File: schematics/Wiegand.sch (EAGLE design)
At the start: 66 parts, among them IC1 MC33269ST-3.3T3, J1 AVR_SPI_PRG_6NS, Q1 NTR1P02T1G, Q2 NTR1P02T1G, U1 ATMEGA168, U2 RS485_SP491, U4 MOC3063, U5 MOC3063, U6 MOC3063, U7 MOC3063, U8 MOC3063, U9 MOC3063, Y1 16Mhz

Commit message: minor changes to board, adding firmware and eagleup render
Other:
- note added: "- 100ohm resistor on head: B---A - 100ohm resistor on slave: Y---Z, B---A CONNECTIONS: - Head-Z --- Slave-B - Head-Y --- Slave-A - Head-A --- Slave-Y - Head-B --- Slave-Z"
- note added: "- add pullup resistors to D0 and D1 (use internal?) - add 0.1uf decoup ceramic near 5v headers - fix and annotate terminal node jumpers and resistors"
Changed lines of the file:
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@@
 <setting verticaltext="up"/>
 </settings>
-<grid distance="0.1" unitdist="inch" unit="inch" style="lines" multiple="1" display="no" altdistance="0.01" altunitdist="inch" altunit="inch"/>
+<grid distance="100" unitdist="mil" unit="mil" style="lines" multiple="1" display="no" altdistance="50" altunitdist="mil" altunit="mil"/>
 <layers>
 <layer number="1" name="Top" color="4" fill="1" visible="no" active="no"/>
@@
 <layer number="108" name="tplace-old" color="10" fill="1" visible="yes" active="yes"/>
 <layer number="109" name="ref-old" color="11" fill="1" visible="yes" active="yes"/>
-<layer number="110" name="fp0" color="7" fill="1" visible="no" active="yes"/>
+<layer number="110" name="fp0" color="7" fill="1" visible="yes" active="yes"/>
 <layer number="116" name="Patch_BOT" color="9" fill="4" visible="yes" active="yes"/>
 <layer number="121" name="_tsilk" color="7" fill="1" visible="yes" active="yes"/>
 <layer number="122" name="_bsilk" color="7" fill="1" visible="yes" active="yes"/>
-<layer number="123" name="tTestmark" color="7" fill="1" visible="no" active="yes"/>
-<layer number="124" name="bTestmark" color="7" fill="1" visible="no" active="yes"/>
-<layer number="125" name="_tNames" color="7" fill="1" visible="no" active="yes"/>
+<layer number="123" name="tTestmark" color="7" fill="1" visible="yes" active="yes"/>
+<layer number="124" name="bTestmark" color="7" fill="1" visible="yes" active="yes"/>
+<layer number="125" name="_tNames" color="7" fill="1" visible="yes" active="yes"/>
 <layer number="131" name="prix" color="7" fill="1" visible="yes" active="yes"/>
 <layer number="132" name="test" color="7" fill="1" visible="yes" active="yes"/>
-<layer number="144" name="Drill_legend" color="7" fill="1" visible="no" active="yes"/>
+<layer number="144" name="Drill_legend" color="7" fill="1" visible="yes" active="yes"/>
 <layer number="151" name="HeatSink" color="7" fill="1" visible="yes" active="yes"/>
-<layer number="199" name="Contour" color="7" fill="1" visible="no" active="yes"/>
+<layer number="199" name="Contour" color="7" fill="1" visible="yes" active="yes"/>
 <layer number="200" name="200bmp" color="1" fill="10" visible="no" active="no"/>
 <layer number="201" name="201bmp" color="2" fill="1" visible="no" active="no"/>
@@
 <layer number="207" name="207bmp" color="8" fill="10" visible="yes" active="yes"/>
 <layer number="208" name="208bmp" color="9" fill="10" visible="yes" active="yes"/>
-<layer number="209" name="209bmp" color="7" fill="1" visible="no" active="yes"/>
-<layer number="210" name="210bmp" color="7" fill="1" visible="no" active="yes"/>
-<layer number="211" name="211bmp" color="7" fill="1" visible="no" active="yes"/>
-<layer number="212" name="212bmp" color="7" fill="1" visible="no" active="yes"/>
-<layer number="213" name="213bmp" color="7" fill="1" visible="no" active="yes"/>
-<layer number="214" name="214bmp" color="7" fill="1" visible="no" active="yes"/>
-<layer number="215" name="215bmp" color="7" fill="1" visible="no" active="yes"/>
-<layer number="216" name="216bmp" color="7" fill="1" visible="no" active="yes"/>
+<layer number="209" name="209bmp" color="7" fill="1" visible="yes" active="yes"/>
+<layer number="210" name="210bmp" color="7" fill="1" visible="yes" active="yes"/>
+<layer number="211" name="211bmp" color="7" fill="1" visible="yes" active="yes"/>
+<layer number="212" name="212bmp" color="7" fill="1" visible="yes" active="yes"/>
+<layer number="213" name="213bmp" color="7" fill="1" visible="yes" active="yes"/>
+<layer number="214" name="214bmp" color="7" fill="1" visible="yes" active="yes"/>
+<layer number="215" name="215bmp" color="7" fill="1" visible="yes" active="yes"/>
+<layer number="216" name="216bmp" color="7" fill="1" visible="yes" active="yes"/>
 <layer number="217" name="217bmp" color="18" fill="1" visible="no" active="no"/>
 <layer number="218" name="218bmp" color="19" fill="1" visible="no" active="no"/>
@@
 <text x="139.7" y="162.56" size="1.778" layer="91" rot="R270">FIRST NODE</text>
 <text x="203.2" y="157.48" size="1.778" layer="91" rot="R270">LAST NODE</text>
+<text x="287.02" y="261.62" size="5.08" layer="91" align="bottom-right">- add pullup resistors to D0 and D1 (use internal?)
+- add 0.1uf decoup ceramic near 5v headers
+- fix and annotate terminal node jumpers and resistors</text>
+<text x="307.34" y="17.78" size="5.08" layer="91">- 100ohm resistor on head: B---A
+- 100ohm resistor on slave: Y---Z, B---A
+CONNECTIONS:
+- Head-Z --- Slave-B
+- Head-Y --- Slave-A
+- Head-A --- Slave-Y
+- Head-B --- Slave-Z</text>
 </plain>
 <instances>

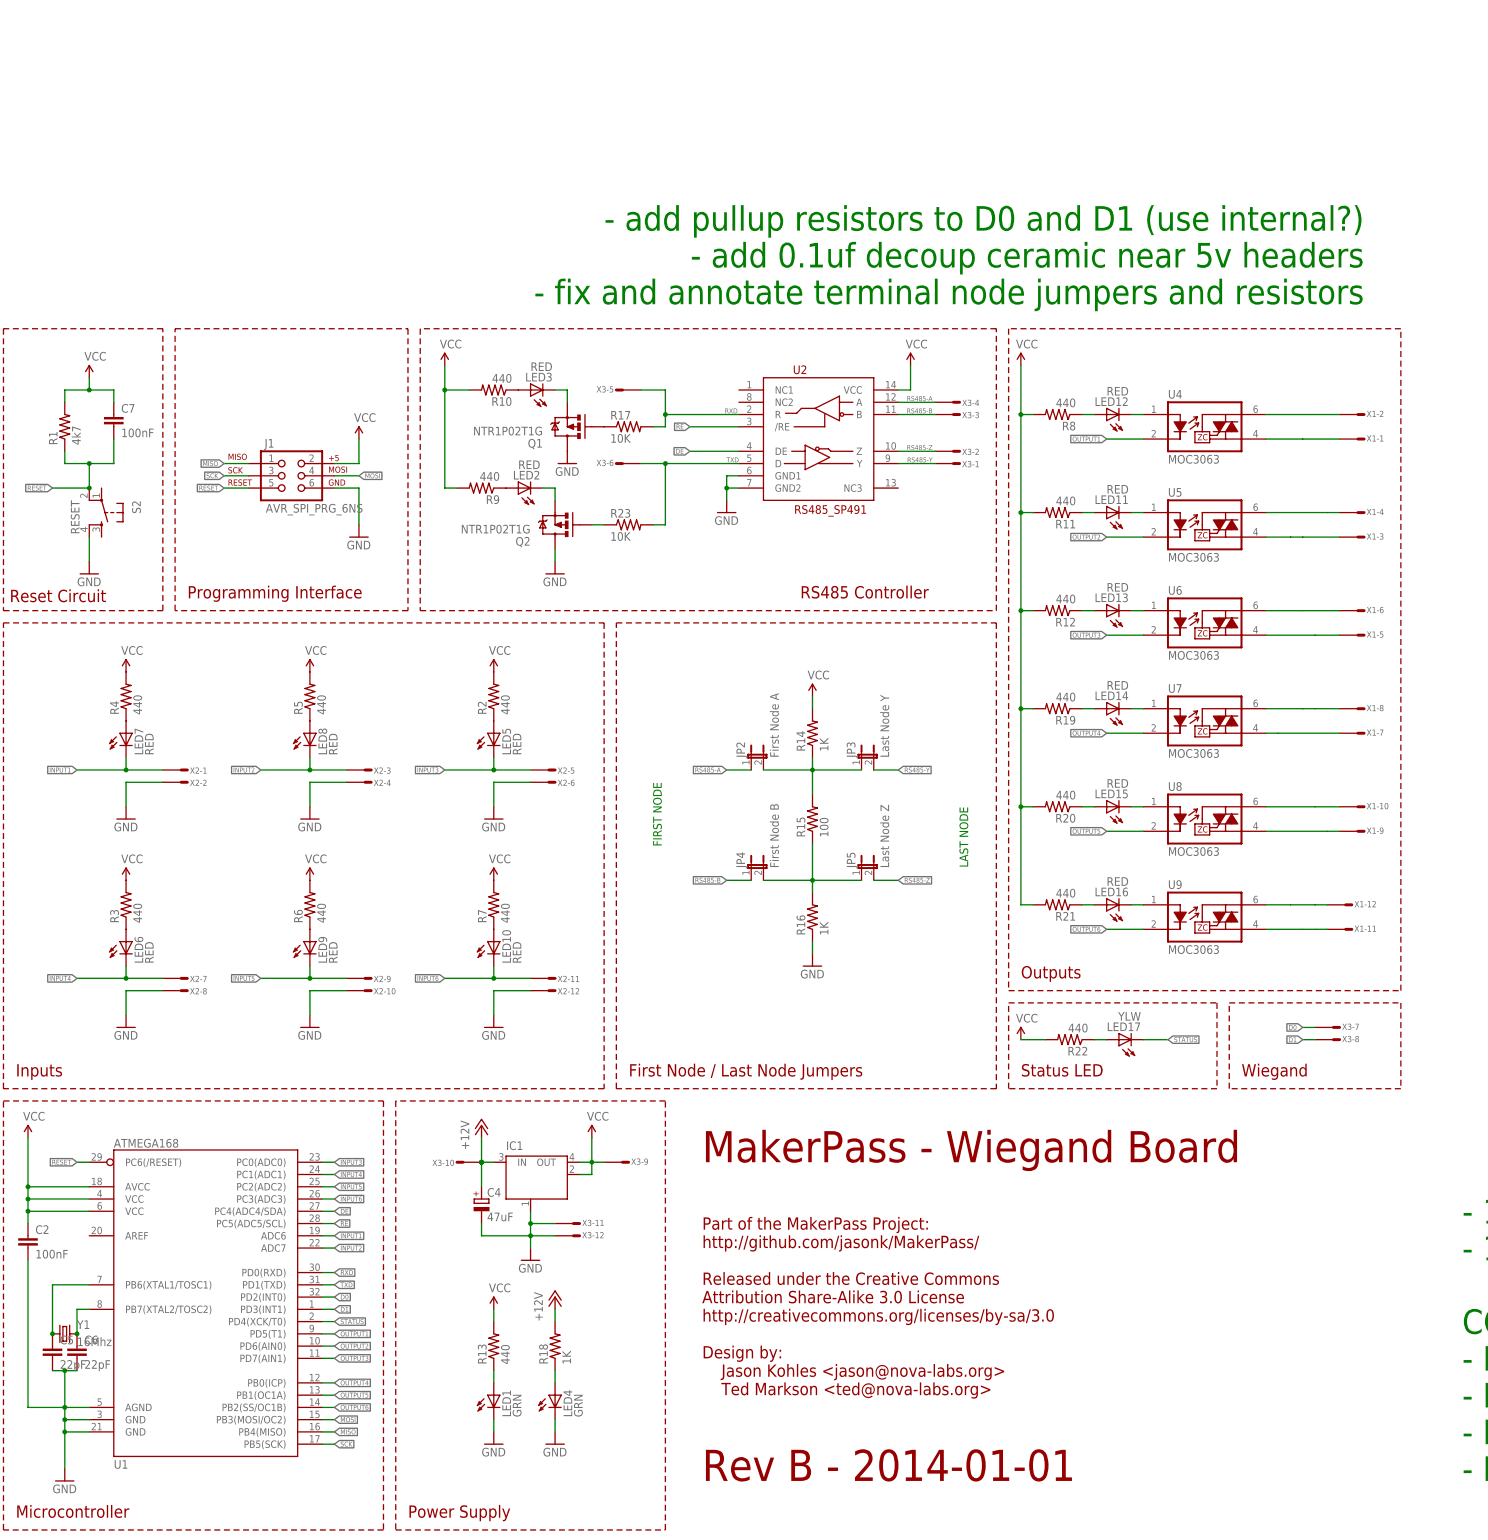
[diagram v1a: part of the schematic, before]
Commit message: minor edits to brd, rerendered eagleup model
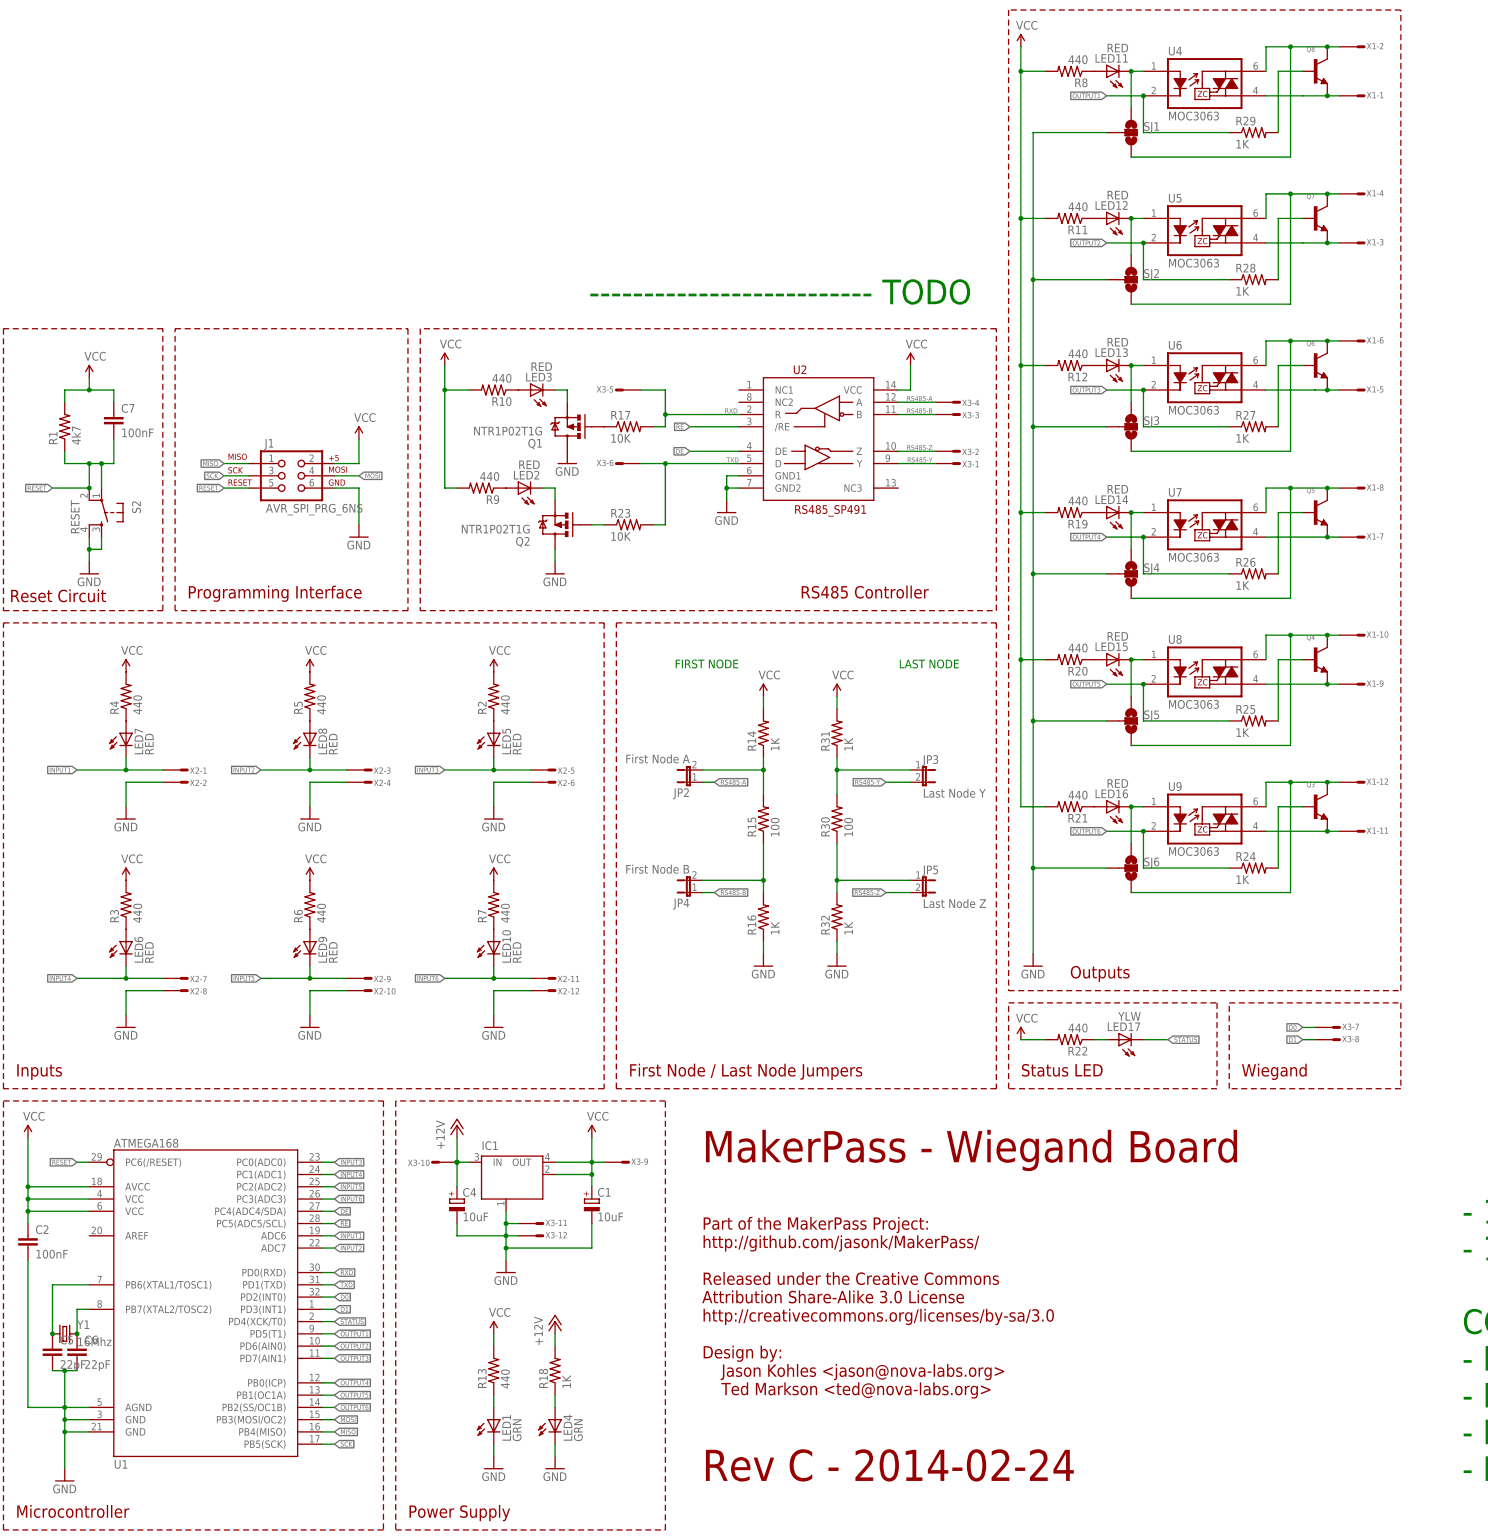
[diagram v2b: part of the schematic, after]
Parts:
- added C1: 10uF, rcl:CPOL-EUD
- added Q3, Q4, Q5, Q6, Q7, Q8: (no value), LumisenseV6:NPN-BEC-SOT23-3
- added R24, R25, R26, R27, R28, R29, R31, R32: 1K, SparkFun:RESISTOR0603-RES
- added R30: 100, SparkFun:RESISTOR0603-RES
- added SJ1, SJ2, SJ3, SJ4, SJ5, SJ6: (no value), SparkFun-Passives:SOLDERJUMPER_2WAYS
- C4: value 47uF -> 10uF; MFG_PN EMVA250ADA470MF55G -> EMVA250ADA100MD55G
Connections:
- removed net N$17: U4.T2, X1-1.S
- new net N$43: Q4.B, R25.2
- new net N$435: Q3.B, R24.2
- new net N$44: Q5.B, R26.2
- new net N$48: Q6.B, R27.2
- new net N$49: Q7.B, R28.2
- new net N$50: Q8.B, R29.2
- new net N$51: JP2.2, R14.1, R15.2
- new net N$52: JP4.2, R15.1, R16.2
- new net N$53: Q8.E, U4.T2, X1-1.S
- net GND: now also C1.-, R32.1, S2.3, SJ1.2, SJ2.2, SJ3.2, SJ4.2, SJ5.2, SJ6.2
- net N$15: now also LED11.C, SJ1.1; no longer LED12.C
- net N$16: now also LED11.A; no longer LED12.A
- net N$18: now also Q8.C, SJ1.3
- net N$19: now also Q7.E
- net N$20: now also Q7.C, SJ2.3
- net N$21: now also LED12.A; no longer LED11.A
- net N$22: now also LED12.C, SJ2.1; no longer LED11.C
- net N$23: now also Q6.E
- net N$24: now also Q6.C, SJ3.3
- net N$28: now also SJ3.1
- net N$29: now also Q5.E
- net N$3: now also Q4.E
- net N$30: now also Q5.C, SJ4.3
- net N$32: now also SJ4.1
- net N$36: now also SJ5.1
- net N$37: now also Q3.C, SJ6.3, U9.T1, X1-12.S; no longer U9.T2, X1-11.S
- net N$38: now also Q3.E, U9.T2, X1-11.S; no longer U9.T1, X1-12.S
- net N$4: now also Q4.C, SJ5.3
- net N$40: now also SJ6.1
- net N$6: now also R30.1, R32.2; no longer JP4.2, R15.1, R16.2
- net N$7: now also R30.2, R31.1; no longer JP2.2, R14.1, R15.2
- net OUTPUT1: now also R29.1
- net OUTPUT2: now also R28.1
- net OUTPUT3: now also R27.1
- net OUTPUT4: now also R26.1
- net OUTPUT5: now also R25.1
- net OUTPUT6: now also R24.1
- net RESET: now also S2.1
- net VCC: now also C1.+, R31.2
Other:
- note added: "-------------------------- TODO"
- note added: "Rev C - 2014-02-24"
- note removed: "- add pullup resistors to D0 and D1 (use internal?) - add 0.1uf decoup ceramic near 5v headers - fix and annotate terminal node jumpers and resistors"
- note removed: "Rev B - 2014-01-01"
- moved on the sheet: C4, IC1, JP2, JP3, JP4, JP5, LED1, LED11, LED12, LED13, LED14, LED15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
